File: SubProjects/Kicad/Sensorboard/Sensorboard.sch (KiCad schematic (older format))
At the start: 30 parts, among them K1 Omron_g5v1, P1 ToyRaceCar_V2_REV3_J4, P2 ToyRaceCar_V2_REV3_J3, P3 ToyRaceCar_V2_REV3_J2, P4 ToyRaceCar_V2_REV3_J1, P5 MPU-6050, P6 ToyRaceCar_V2_REV3_J5, P7 CONN_01X02, P8 SS495A, P9 CNY70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

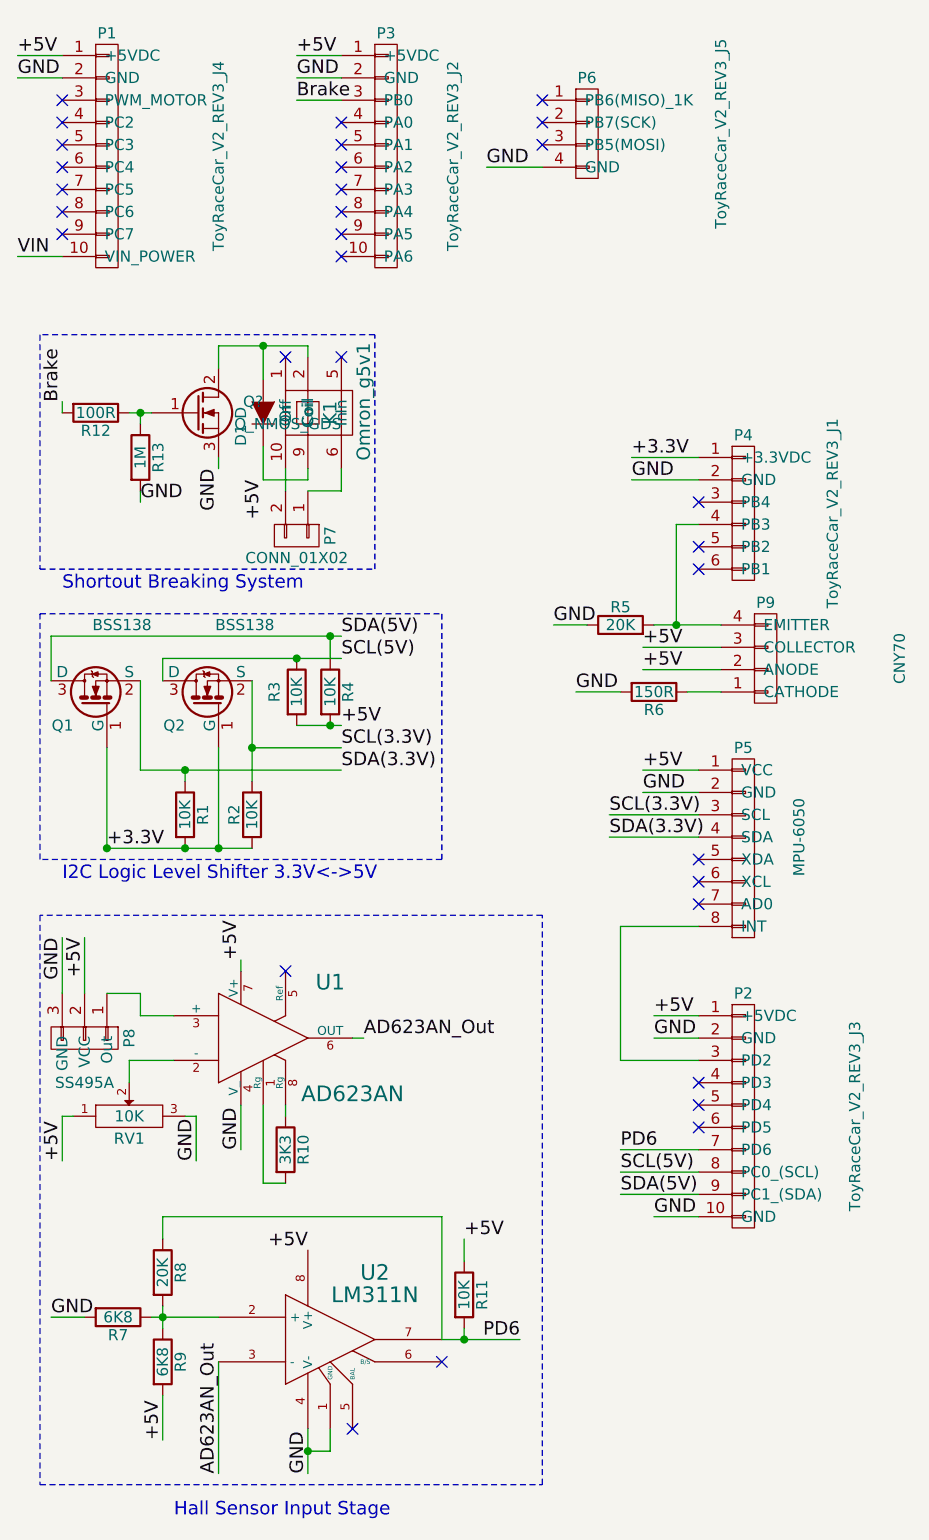
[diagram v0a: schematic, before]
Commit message: Working sensor board REV 2.
-error, Flipped the footprint for the relay
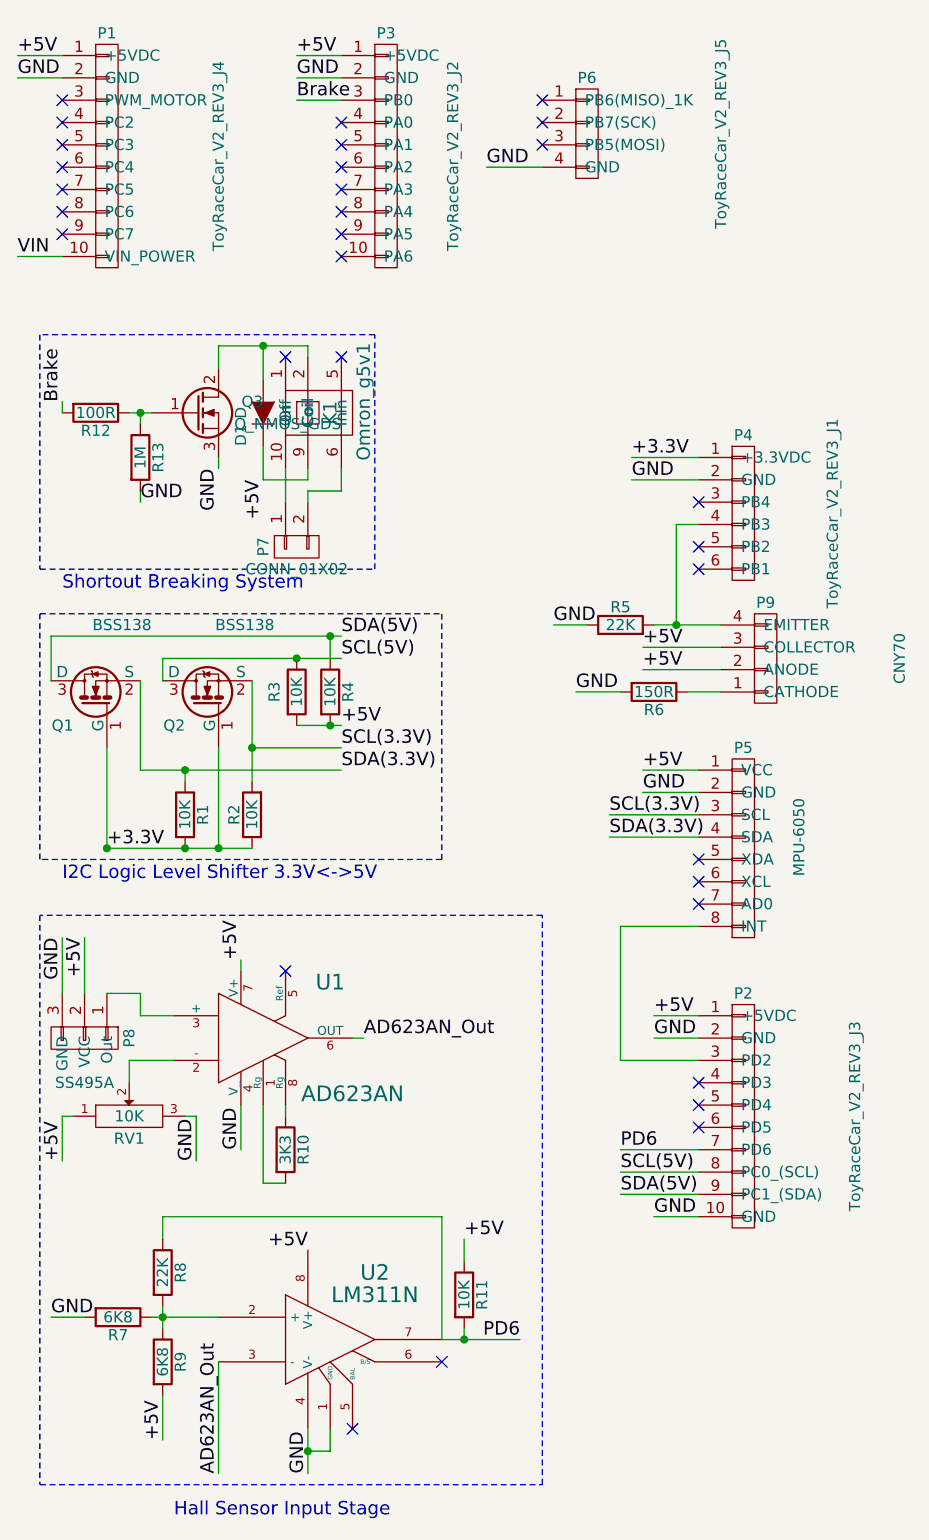
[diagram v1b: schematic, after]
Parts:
- P7: footprint Sensorboard:KK254-4 -> Pin_Headers:Pin_Header_Angled_1x02
- Q3: renamed from Q?; footprint (none) -> Sensorboard:CASE369D
- R5, R8: value 20K -> 22K
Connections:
- net at K1.10 (On): now also P7.1 (P1); no longer P7.2 (P2)
- net at K1.6 (In): now also P7.2 (P2); no longer P7.1 (P1)
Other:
- moved on the sheet: P7
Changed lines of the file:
@@
 P 3250 3250
 F 0 "R5" V 3330 3250 50  0000 C CNN
-F 1 "20K" V 3250 3250 50  0000 C CNN
+F 1 "22K" V 3250 3250 50  0000 C CNN
 F 2 "Resistors_SMD:R_0805_HandSoldering" V 3180 3250 30  0001 C CNN
 F 3 "" H 3250 3250 30  0000 C CNN
@@
 P 1200 6150
 F 0 "R8" V 1280 6150 50  0000 C CNN
-F 1 "20K" V 1200 6150 50  0000 C CNN
+F 1 "22K" V 1200 6150 50  0000 C CNN
 F 2 "Resistors_SMD:R_0805_HandSoldering" V 1130 6150 30  0001 C CNN
 F 3 "" H 1200 6150 30  0000 C CNN
@@
 L CONN_01X02 P7
 U 1 1 55616D13
-P 1800 2850
-F 0 "P7" H 1800 3000 50  0000 C CNN
-F 1 "CONN_01X02" V 1900 2850 50  0000 C CNN
-F 2 "Sensorboard:KK254-4" H 1800 2850 60  0001 C CNN
-F 3 "" H 1800 2850 60  0000 C CNN
-	1    1800 2850
-	0    1    1    0
+P 1800 2900
+F 0 "P7" H 1800 3050 50  0000 C CNN
+F 1 "CONN_01X02" V 1900 2900 50  0000 C CNN
+F 2 "Pin_Headers:Pin_Header_Angled_1x02" H 1800 2900 60  0001 C CNN
+F 3 "" H 1800 2900 60  0000 C CNN
+	1    1800 2900
+	0    -1   1    0
 $EndComp
 NoConn ~ 2000 2050
@@
 GND
 Wire Wire Line
-	1750 2550 1750 2650
+	1750 2550 1750 2700
 Wire Wire Line
 	1850 2650 2000 2650
@@
 Shortout Breaking System
 $Comp
-L Q_NMOS_GDS Q?
+L Q_NMOS_GDS Q3
 U 1 1 55620FAF
 P 1350 2300
-F 0 "Q?" H 1650 2350 50  0000 R CNN
+F 0 "Q3" H 1650 2350 50  0000 R CNN
 F 1 "Q_NMOS_GDS" H 2000 2250 50  0000 R CNN
-F 2 "" H 1550 2400 29  0000 C CNN
+F 2 "Sensorboard:CASE369D" H 1550 2400 29  0001 C CNN
 F 3 "" H 1350 2300 60  0000 C CNN
 	1    1350 2300
@@
 Wire Wire Line
 	1450 2550 1450 2500
+Wire Wire Line
+	1850 2650 1850 2700
 $EndSCHEMATC
